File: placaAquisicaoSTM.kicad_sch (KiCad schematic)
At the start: 4 parts

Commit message: Removi as entradas analógicas, projeto delas estava errado
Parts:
- H1, H2, H3, H4: footprint (none) -> MountingHole:MountingHole_4.3mm_M4_DIN965_Pad
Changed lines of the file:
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@@
 			)
 		)
-		(property "Footprint" ""
+		(property "Footprint" "MountingHole:MountingHole_4.3mm_M4_DIN965_Pad"
 			(at 109.22 142.24 0)
 			(effects
@@
 			)
 		)
-		(property "Footprint" ""
+		(property "Footprint" "MountingHole:MountingHole_4.3mm_M4_DIN965_Pad"
 			(at 81.28 142.24 0)
 			(effects
@@
 			)
 		)
-		(property "Footprint" ""
+		(property "Footprint" "MountingHole:MountingHole_4.3mm_M4_DIN965_Pad"
 			(at 109.22 133.35 0)
 			(effects
@@
 			)
 		)
-		(property "Footprint" ""
+		(property "Footprint" "MountingHole:MountingHole_4.3mm_M4_DIN965_Pad"
 			(at 81.28 133.35 0)
 			(effects

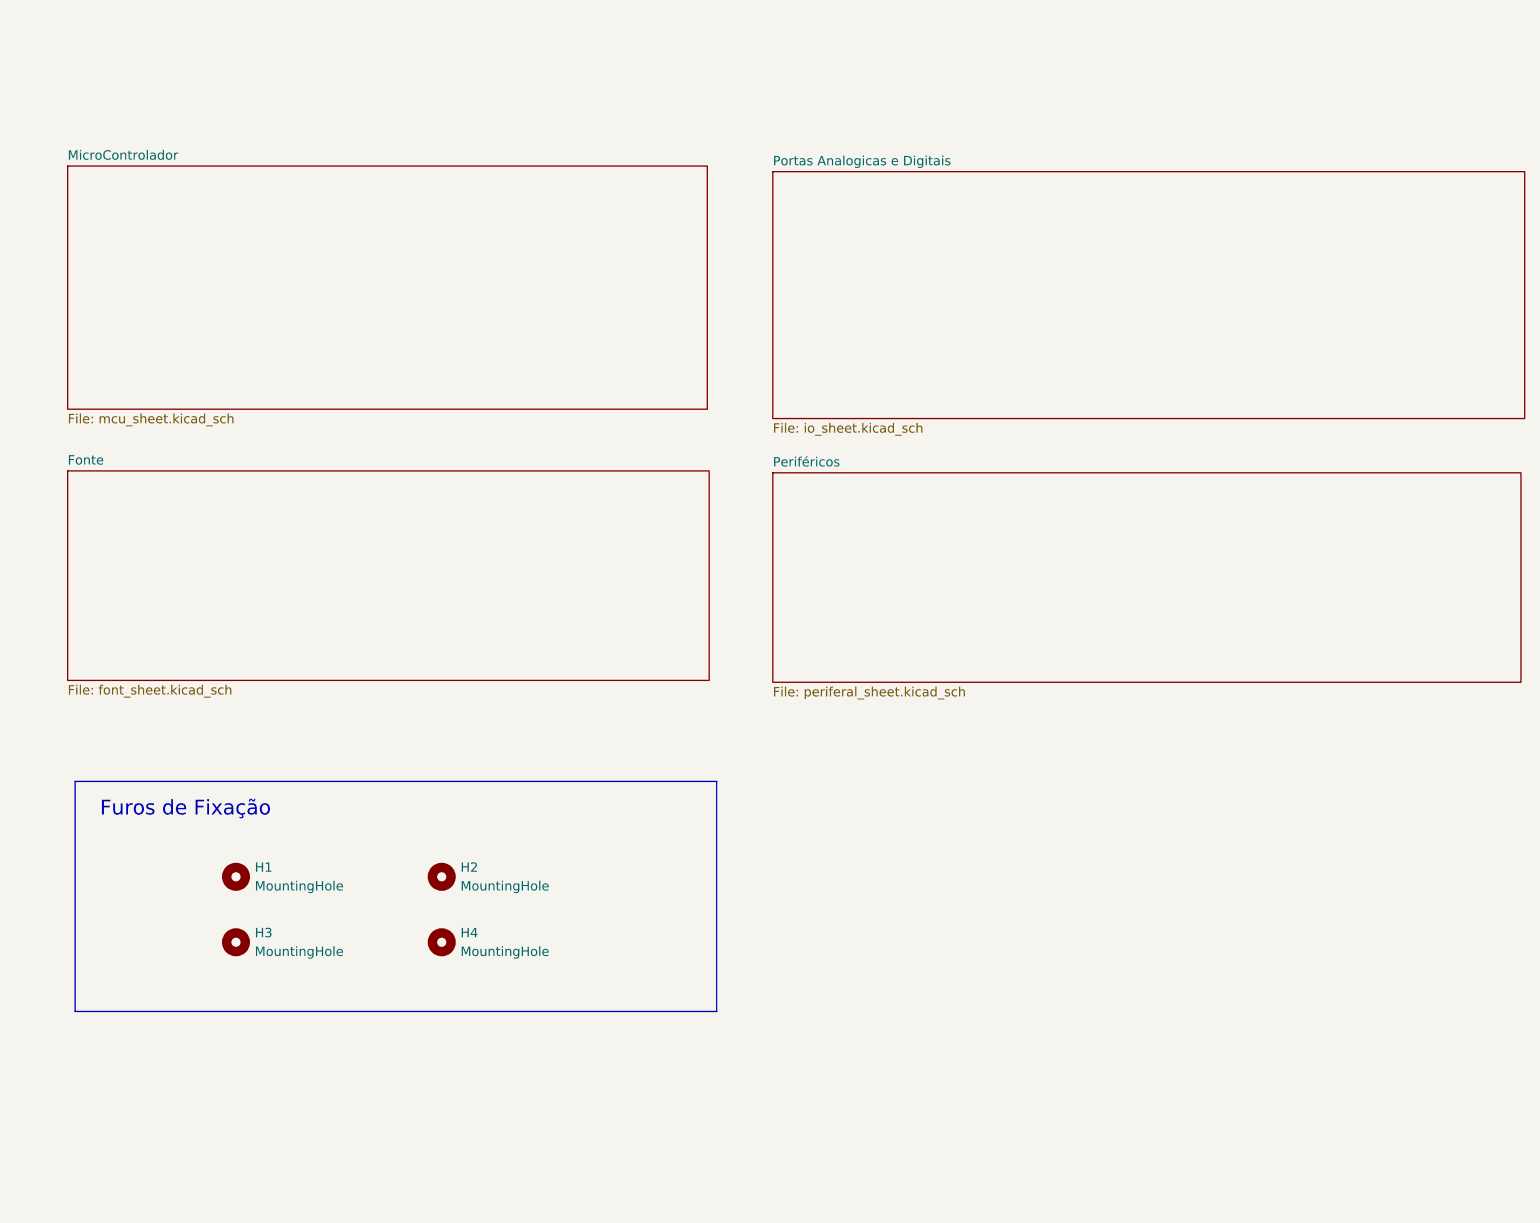
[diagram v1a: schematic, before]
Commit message: Alterei para ter 3 portas analogicas, adaptei o circuito do RPM para ter um jumper que permite usar como entrada digital
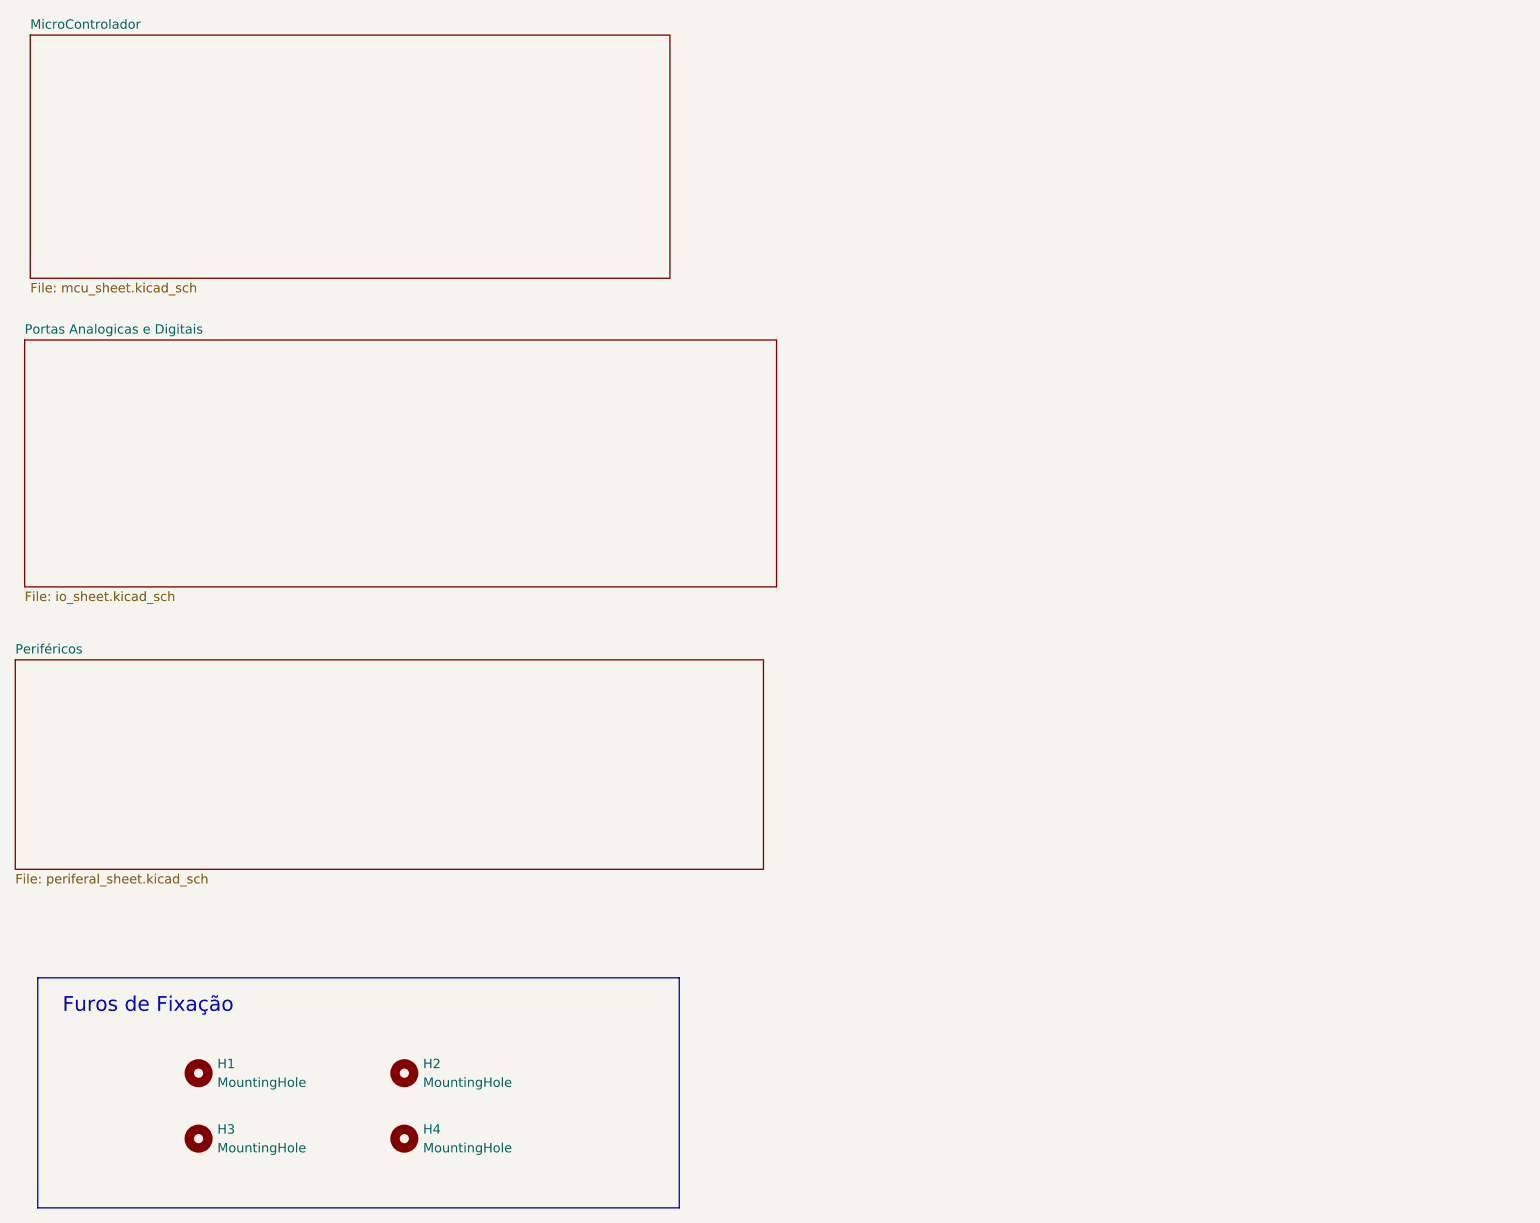
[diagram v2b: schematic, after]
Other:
- removed sheet Fonte
- moved on the sheet: H1, H2, H3, H4
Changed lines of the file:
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@@
 	(paper "A4")
 	(rectangle
-		(start 59.436 120.396)
-		(end 146.558 151.638)
+		(start 54.356 147.066)
+		(end 141.478 178.308)
 		(stroke
 			(width 0)
@@
 	(text "Furos de Fixação"
 		(exclude_from_sim no)
-		(at 74.422 124.206 0)
+		(at 69.342 150.876 0)
 		(effects
 			(font
@@
 	(symbol
 		(lib_id "Mechanical:MountingHole")
-		(at 109.22 142.24 0)
+		(at 104.14 168.91 0)
 		(unit 1)
 		(exclude_from_sim no)
@@
 		(fields_autoplaced yes)
 		(property "Reference" "H4"
-			(at 111.76 140.9699 0)
+			(at 106.68 167.6399 0)
 			(effects
 				(font
@@
 		)
 		(property "Value" "MountingHole"
-			(at 111.76 143.5099 0)
+			(at 106.68 170.1799 0)
 			(effects
 				(font
@@
 		)
 		(property "Footprint" "MountingHole:MountingHole_4.3mm_M4_DIN965_Pad"
-			(at 109.22 142.24 0)
+			(at 104.14 168.91 0)
 			(effects
 				(font
@@
 		)
 		(property "Datasheet" "~"
-			(at 109.22 142.24 0)
+			(at 104.14 168.91 0)
 			(effects
 				(font
@@
 		)
 		(property "Description" "Mounting Hole without connection"
-			(at 109.22 142.24 0)
+			(at 104.14 168.91 0)
 			(effects
 				(font
@@
 	(symbol
 		(lib_id "Mechanical:MountingHole")
-		(at 81.28 142.24 0)
+		(at 76.2 168.91 0)
 		(unit 1)
 		(exclude_from_sim no)
@@
 		(fields_autoplaced yes)
 		(property "Reference" "H3"
-			(at 83.82 140.9699 0)
+			(at 78.74 167.6399 0)
 			(effects
 				(font
@@
 		)
 		(property "Value" "MountingHole"
-			(at 83.82 143.5099 0)
+			(at 78.74 170.1799 0)
 			(effects
 				(font
@@
 		)
 		(property "Footprint" "MountingHole:MountingHole_4.3mm_M4_DIN965_Pad"
-			(at 81.28 142.24 0)
+			(at 76.2 168.91 0)
 			(effects
 				(font
@@
 		)
 		(property "Datasheet" "~"
-			(at 81.28 142.24 0)
+			(at 76.2 168.91 0)
 			(effects
 				(font
@@
 		)
 		(property "Description" "Mounting Hole without connection"
-			(at 81.28 142.24 0)
+			(at 76.2 168.91 0)
 			(effects
 				(font
@@
 	(symbol
 		(lib_id "Mechanical:MountingHole")
-		(at 109.22 133.35 0)
+		(at 104.14 160.02 0)
 		(unit 1)
 		(exclude_from_sim no)
@@
 		(fields_autoplaced yes)
 		(property "Reference" "H2"
-			(at 111.76 132.0799 0)
+			(at 106.68 158.7499 0)
 			(effects
 				(font
@@
 		)
 		(property "Value" "MountingHole"
-			(at 111.76 134.6199 0)
+			(at 106.68 161.2899 0)
 			(effects
 				(font
@@
 		)
 		(property "Footprint" "MountingHole:MountingHole_4.3mm_M4_DIN965_Pad"
-			(at 109.22 133.35 0)
+			(at 104.14 160.02 0)
 			(effects
 				(font
@@
 		)
 		(property "Datasheet" "~"
-			(at 109.22 133.35 0)
+			(at 104.14 160.02 0)
 			(effects
 				(font
@@
 		)
 		(property "Description" "Mounting Hole without connection"
-			(at 109.22 133.35 0)
+			(at 104.14 160.02 0)
 			(effects
 				(font
@@
 	(symbol
 		(lib_id "Mechanical:MountingHole")
-		(at 81.28 133.35 0)
+		(at 76.2 160.02 0)
 		(unit 1)
 		(exclude_from_sim no)
@@
 		(fields_autoplaced yes)
 		(property "Reference" "H1"
-			(at 83.82 132.0799 0)
+			(at 78.74 158.7499 0)
 			(effects
 				(font
@@
 		)
 		(property "Value" "MountingHole"
-			(at 83.82 134.6199 0)
+			(at 78.74 161.2899 0)
 			(effects
 				(font
@@
 		)
 		(property "Footprint" "MountingHole:MountingHole_4.3mm_M4_DIN965_Pad"
-			(at 81.28 133.35 0)
+			(at 76.2 160.02 0)
 			(effects
 				(font
@@
 		)
 		(property "Datasheet" "~"
-			(at 81.28 133.35 0)
+			(at 76.2 160.02 0)
 			(effects
 				(font
@@
 		)
 		(property "Description" "Mounting Hole without connection"
-			(at 81.28 133.35 0)
+			(at 76.2 160.02 0)
 			(effects
 				(font
@@
 	)
 	(sheet
-		(at 154.178 78.486)
+		(at 51.308 103.886)
 		(size 101.6 28.448)
 		(fields_autoplaced yes)
@@
 		)
 		(property "Sheetname" "Periféricos"
-			(at 154.178 77.7744 0)
+			(at 51.308 103.1744 0)
 			(effects
 				(font
@@
 		)
 		(property "Sheetfile" "periferal_sheet.kicad_sch"
-			(at 154.178 107.5186 0)
+			(at 51.308 132.9186 0)
 			(effects
 				(font
@@
 	)
 	(sheet
-		(at 58.42 36.83)
+		(at 53.34 19.05)
 		(size 86.868 33.02)
 		(fields_autoplaced yes)
@@
 		)
 		(property "Sheetname" "MicroControlador"
-			(at 58.42 36.1184 0)
+			(at 53.34 18.3384 0)
 			(effects
 				(font
@@
 		)
 		(property "Sheetfile" "mcu_sheet.kicad_sch"
-			(at 58.42 70.4346 0)
+			(at 53.34 52.6546 0)
 			(effects
 				(font
@@
 	)
 	(sheet
-		(at 58.42 78.232)
-		(size 87.122 28.448)
+		(at 52.578 60.452)
+		(size 102.108 33.528)
 		(fields_autoplaced yes)
 		(stroke
@@
 			(color 0 0 0 0.0000)
 		)
-		(property "Sheetname" "Fonte"
-			(at 58.42 77.5204 0)
+		(property "Sheetname" "Portas Analogicas e Digitais"
+			(at 52.578 59.7404 0)
 			(effects
 				(font
@@
 			)
 		)
-		(property "Sheetfile" "font_sheet.kicad_sch"
-			(at 58.42 107.2646 0)
-			(effects
-				(font
-					(size 1.27 1.27)
-				)
-				(justify left top)
-			)
-		)
-		(instances
-			(project "placaAquisicaoSTM"
-				(path "/089184b8-f600-4584-b3f1-b59eb16eefc1"
-					(page "4")
-				)
-			)
-		)
-	)
-	(sheet
-		(at 154.178 37.592)
-		(size 102.108 33.528)
-		(fields_autoplaced yes)
-		(stroke
-			(width 0.1524)
-			(type solid)
-		)
-		(fill
-			(color 0 0 0 0.0000)
-		)
-		(property "Sheetname" "Portas Analogicas e Digitais"
-			(at 154.178 36.8804 0)
-			(effects
-				(font
-					(size 1.27 1.27)
-				)
-				(justify left bottom)
-			)
-		)
 		(property "Sheetfile" "io_sheet.kicad_sch"
-			(at 154.178 71.7046 0)
-			(effects
-				(font
+			(at 52.578 94.5646 0)
+			(effects
+				(font
